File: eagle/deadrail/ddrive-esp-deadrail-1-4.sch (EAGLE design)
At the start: 20 parts, among them Q1 BSS123, Q2 BSS123, Q3 BSS123, Q4 BSS123

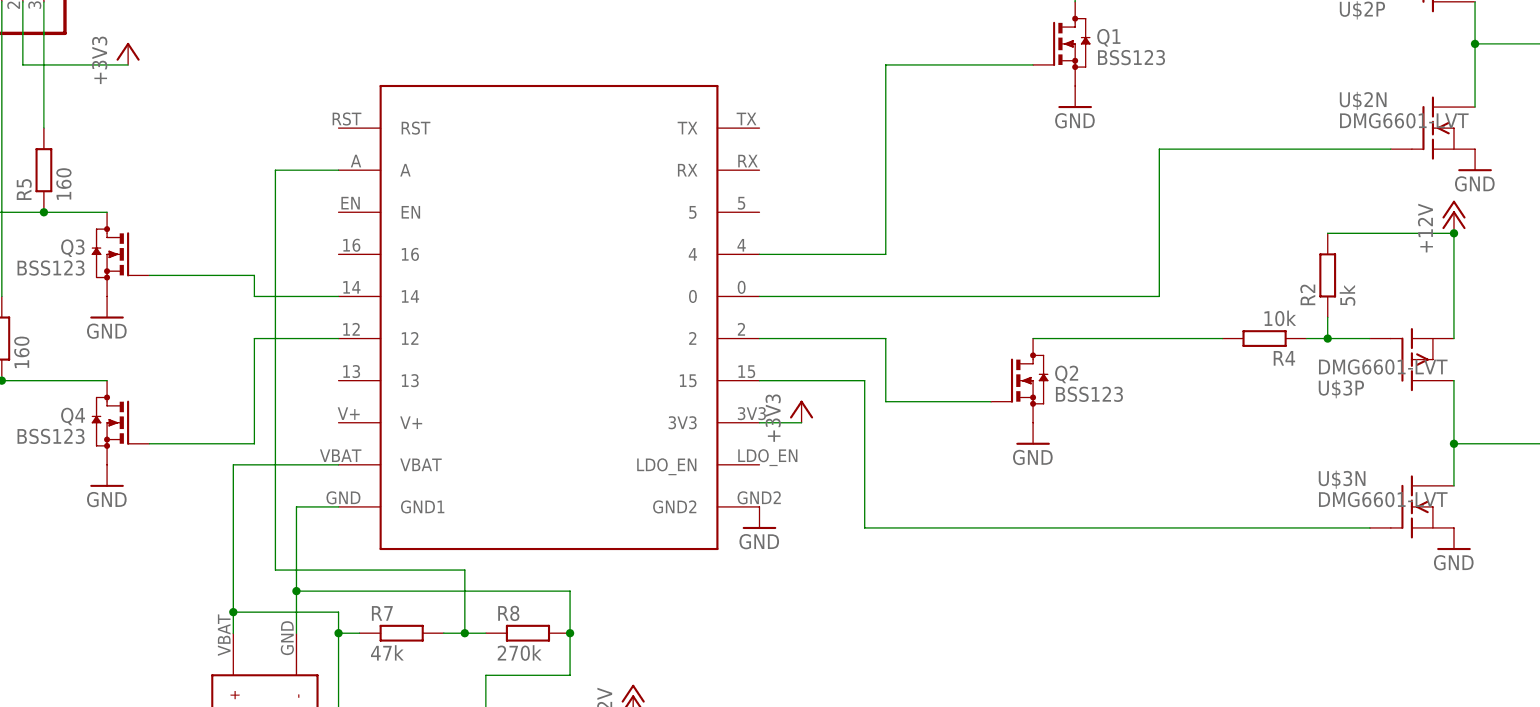
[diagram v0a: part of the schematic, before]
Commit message: Adds all intermediate and the final schematic and board layout for the huzzah baseboard for esp-12 train decoder.
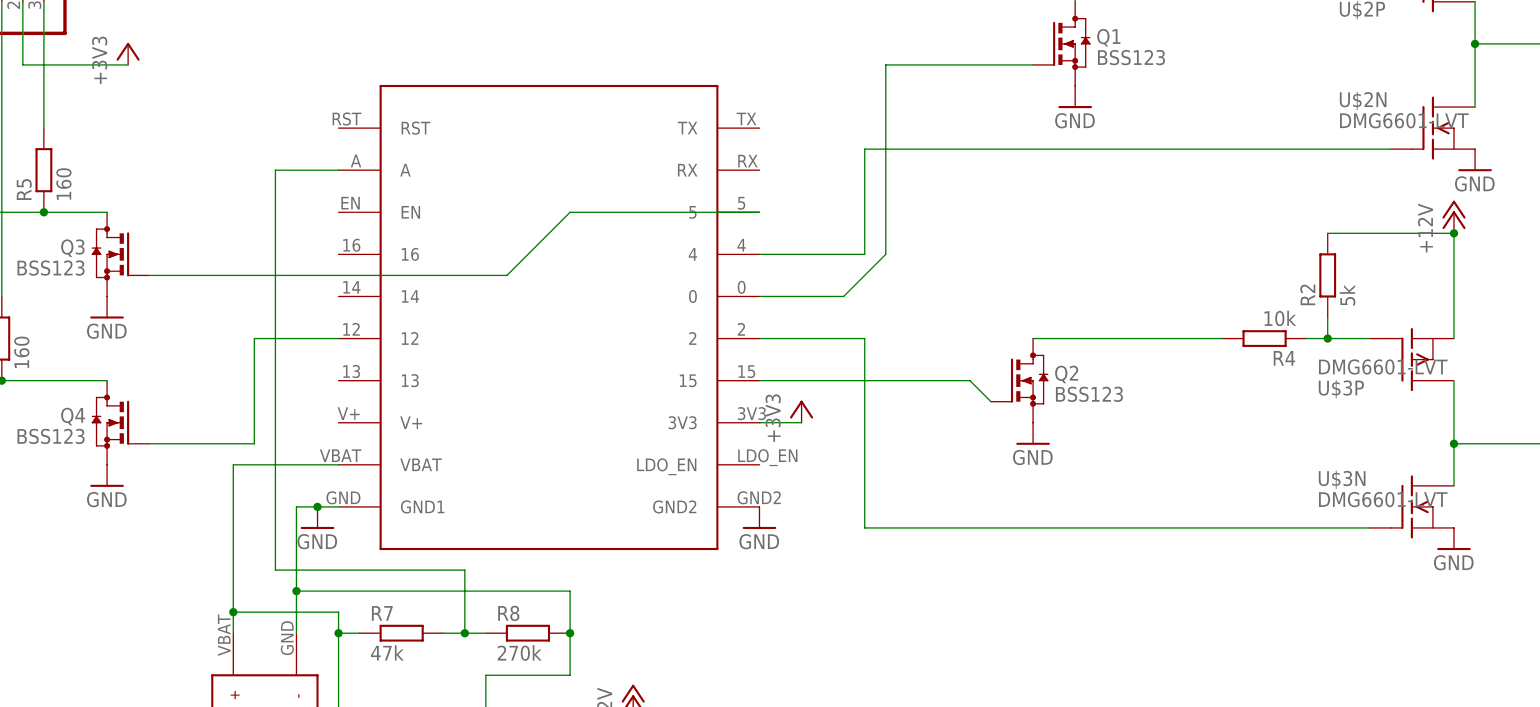
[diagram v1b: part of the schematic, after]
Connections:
- removed net GND1: R8.2, U$1.GND1, U$4.P$1, U$5.GND
- net GND: now also R8.2, U$1.GND1, U$4.P$1, U$5.GND
- net N$10: now also U$1.2; no longer U$1.15
- net N$11: now also U$1.5; no longer U$1.14
- net N$5: now also U$1.0; no longer U$1.4
- net N$8: now also U$1.4; no longer U$1.0
- net N$9: now also U$1.15; no longer U$1.2
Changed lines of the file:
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@@
 <part name="U$5" library="trainlib" deviceset="POLOLU-VREG12" device=""/>
 <part name="P+4" library="supply1" deviceset="+12V" device=""/>
+<part name="GND8" library="supply1" deviceset="GND" device=""/>
 </parts>
 <sheets>
@@
 <instance part="U$5" gate="G$1" x="45.72" y="-22.86" rot="MR180"/>
 <instance part="P+4" gate="1" x="63.5" y="-2.54"/>
+<instance part="GND8" gate="1" x="25.4" y="17.78"/>
 </instances>
 <busses>
@@
 <pinref part="GND7" gate="1" pin="GND"/>
 </segment>
+<segment>
+<pinref part="U$4" gate="G$1" pin="P$1"/>
+<wire x1="22.86" y1="5.08" x2="22.86" y2="10.16" width="0.1524" layer="91"/>
+<pinref part="U$1" gate="G" pin="GND1"/>
+<wire x1="22.86" y1="10.16" x2="22.86" y2="20.32" width="0.1524" layer="91"/>
+<wire x1="22.86" y1="20.32" x2="25.4" y2="20.32" width="0.1524" layer="91"/>
+<pinref part="R8" gate="G$1" pin="2"/>
+<wire x1="25.4" y1="20.32" x2="27.94" y2="20.32" width="0.1524" layer="91"/>
+<wire x1="55.88" y1="5.08" x2="55.88" y2="10.16" width="0.1524" layer="91"/>
+<wire x1="55.88" y1="10.16" x2="22.86" y2="10.16" width="0.1524" layer="91"/>
+<junction x="22.86" y="10.16"/>
+<wire x1="55.88" y1="5.08" x2="55.88" y2="0" width="0.1524" layer="91"/>
+<junction x="55.88" y="5.08"/>
+<pinref part="U$5" gate="G$1" pin="GND"/>
+<wire x1="55.88" y1="0" x2="45.72" y2="0" width="0.1524" layer="91"/>
+<wire x1="45.72" y1="0" x2="45.72" y2="-10.16" width="0.1524" layer="91"/>
+<pinref part="GND8" gate="1" pin="GND"/>
+<junction x="25.4" y="20.32"/>
+</segment>
 </net>
 <net name="N$2" class="0">
@@
 <wire x1="111.76" y1="73.66" x2="93.98" y2="73.66" width="0.1524" layer="91"/>
 <wire x1="93.98" y1="73.66" x2="93.98" y2="50.8" width="0.1524" layer="91"/>
+<pinref part="U$1" gate="G" pin="0"/>
+<wire x1="93.98" y1="50.8" x2="88.9" y2="45.72" width="0.1524" layer="91"/>
+<wire x1="88.9" y1="45.72" x2="78.74" y2="45.72" width="0.1524" layer="91"/>
+</segment>
+</net>
+<net name="N$8" class="0">
+<segment>
+<pinref part="U$2" gate="N" pin="G"/>
+<wire x1="154.94" y1="63.5" x2="91.44" y2="63.5" width="0.1524" layer="91"/>
+<wire x1="91.44" y1="63.5" x2="91.44" y2="50.8" width="0.1524" layer="91"/>
 <pinref part="U$1" gate="G" pin="4"/>
-<wire x1="93.98" y1="50.8" x2="78.74" y2="50.8" width="0.1524" layer="91"/>
-</segment>
-</net>
-<net name="N$8" class="0">
-<segment>
-<pinref part="U$2" gate="N" pin="G"/>
-<wire x1="154.94" y1="63.5" x2="127" y2="63.5" width="0.1524" layer="91"/>
-<wire x1="127" y1="63.5" x2="127" y2="45.72" width="0.1524" layer="91"/>
-<pinref part="U$1" gate="G" pin="0"/>
-<wire x1="127" y1="45.72" x2="78.74" y2="45.72" width="0.1524" layer="91"/>
-</segment>
-</net>
-<net name="N$9" class="0">
-<segment>
-<pinref part="Q2" gate="G$1" pin="G"/>
-<wire x1="106.68" y1="33.02" x2="93.98" y2="33.02" width="0.1524" layer="91"/>
-<wire x1="93.98" y1="33.02" x2="93.98" y2="40.64" width="0.1524" layer="91"/>
-<pinref part="U$1" gate="G" pin="2"/>
-<wire x1="93.98" y1="40.64" x2="78.74" y2="40.64" width="0.1524" layer="91"/>
+<wire x1="91.44" y1="50.8" x2="78.74" y2="50.8" width="0.1524" layer="91"/>
 </segment>
 </net>
@@
 <pinref part="U$3" gate="N" pin="G"/>
 <wire x1="152.4" y1="17.78" x2="91.44" y2="17.78" width="0.1524" layer="91"/>
-<wire x1="91.44" y1="17.78" x2="91.44" y2="35.56" width="0.1524" layer="91"/>
-<pinref part="U$1" gate="G" pin="15"/>
-<wire x1="91.44" y1="35.56" x2="78.74" y2="35.56" width="0.1524" layer="91"/>
+<wire x1="91.44" y1="17.78" x2="91.44" y2="40.64" width="0.1524" layer="91"/>
+<pinref part="U$1" gate="G" pin="2"/>
+<wire x1="91.44" y1="40.64" x2="78.74" y2="40.64" width="0.1524" layer="91"/>
 </segment>
 </net>
@@
 <segment>
 <pinref part="Q3" gate="G$1" pin="G"/>
-<wire x1="5.08" y1="48.26" x2="17.78" y2="48.26" width="0.1524" layer="91"/>
-<wire x1="17.78" y1="48.26" x2="17.78" y2="45.72" width="0.1524" layer="91"/>
-<pinref part="U$1" gate="G" pin="14"/>
-<wire x1="17.78" y1="45.72" x2="27.94" y2="45.72" width="0.1524" layer="91"/>
+<wire x1="5.08" y1="48.26" x2="48.26" y2="48.26" width="0.1524" layer="91"/>
+<pinref part="U$1" gate="G" pin="5"/>
+<wire x1="48.26" y1="48.26" x2="55.88" y2="55.88" width="0.1524" layer="91"/>
+<wire x1="55.88" y1="55.88" x2="78.74" y2="55.88" width="0.1524" layer="91"/>
 </segment>
 </net>
@@
 <pinref part="+3V2" gate="G$1" pin="+3V3"/>
 <wire x1="78.74" y1="30.48" x2="83.82" y2="30.48" width="0.1524" layer="91"/>
-</segment>
-</net>
-<net name="GND1" class="0">
-<segment>
-<pinref part="U$4" gate="G$1" pin="P$1"/>
-<wire x1="22.86" y1="5.08" x2="22.86" y2="10.16" width="0.1524" layer="91"/>
-<pinref part="U$1" gate="G" pin="GND1"/>
-<wire x1="22.86" y1="10.16" x2="22.86" y2="20.32" width="0.1524" layer="91"/>
-<wire x1="22.86" y1="20.32" x2="27.94" y2="20.32" width="0.1524" layer="91"/>
-<pinref part="R8" gate="G$1" pin="2"/>
-<wire x1="55.88" y1="5.08" x2="55.88" y2="10.16" width="0.1524" layer="91"/>
-<wire x1="55.88" y1="10.16" x2="22.86" y2="10.16" width="0.1524" layer="91"/>
-<junction x="22.86" y="10.16"/>
-<wire x1="55.88" y1="5.08" x2="55.88" y2="0" width="0.1524" layer="91"/>
-<junction x="55.88" y="5.08"/>
-<pinref part="U$5" gate="G$1" pin="GND"/>
-<wire x1="55.88" y1="0" x2="45.72" y2="0" width="0.1524" layer="91"/>
-<wire x1="45.72" y1="0" x2="45.72" y2="-10.16" width="0.1524" layer="91"/>
 </segment>
 </net>
@@
 </segment>
 </net>
+<net name="N$9" class="0">
+<segment>
+<pinref part="Q2" gate="G$1" pin="G"/>
+<pinref part="U$1" gate="G" pin="15"/>
+<wire x1="106.68" y1="33.02" x2="104.14" y2="35.56" width="0.1524" layer="91"/>
+<wire x1="104.14" y1="35.56" x2="78.74" y2="35.56" width="0.1524" layer="91"/>
+</segment>
+</net>
